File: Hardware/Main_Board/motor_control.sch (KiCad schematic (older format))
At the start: 22 parts

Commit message: [HARDWARE] Complete the SWD design, remove two undrived motor interfaces
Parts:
- removed P? (x2): CONN_4, symbol CONN_4
- removed P? (x2): CONN_6, symbol CONN_6
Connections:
- net labels removed: DIR3, DIR4, MOTOR_EN3, MOTOR_EN4, PWM3, PWM4, enc3_A, enc3_B, enc4_A, enc4_B
- wire segments 120 -> 90
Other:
- moved on the sheet: P?

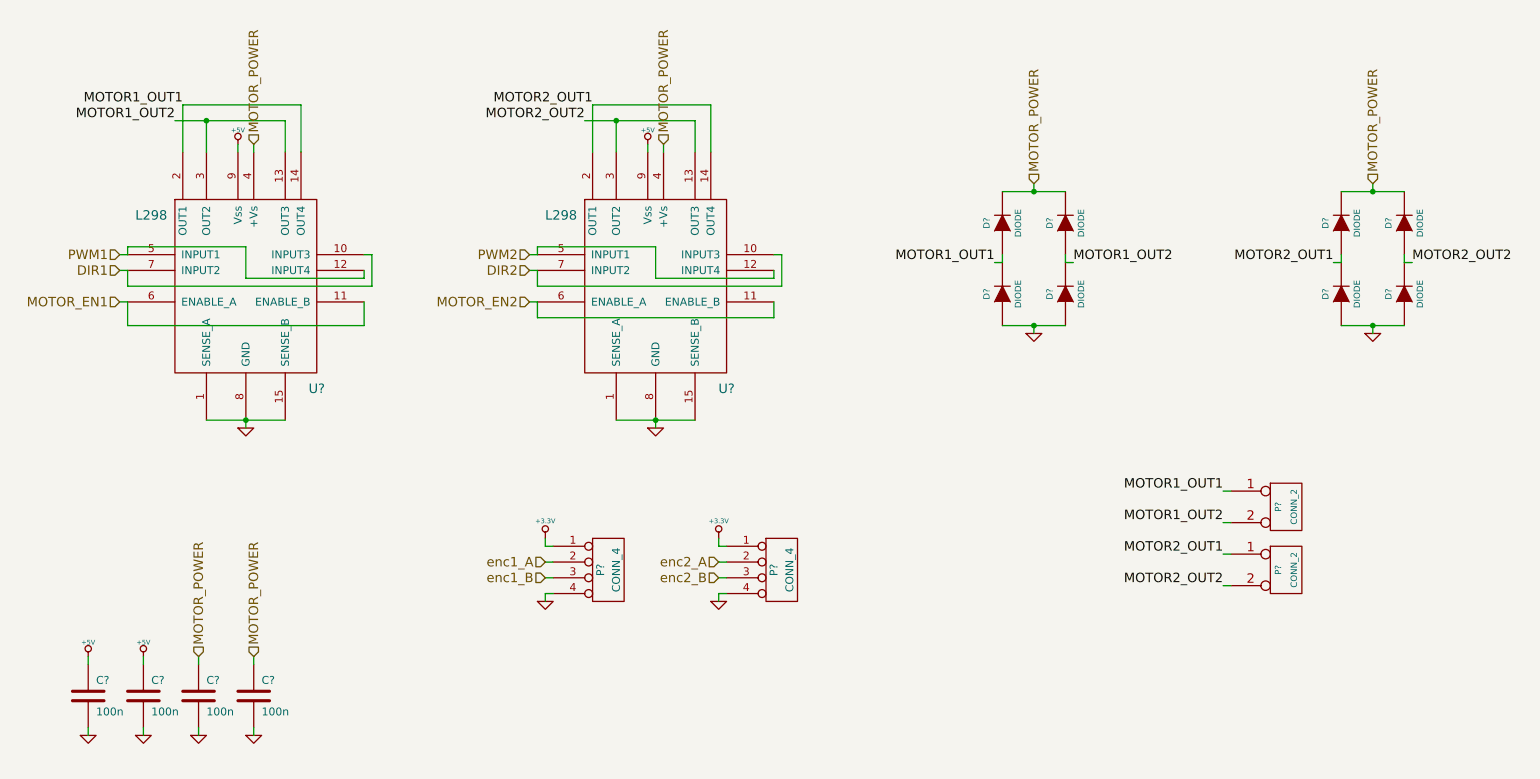
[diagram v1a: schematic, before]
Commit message: [HARDWARE] Component association + schematic modifications
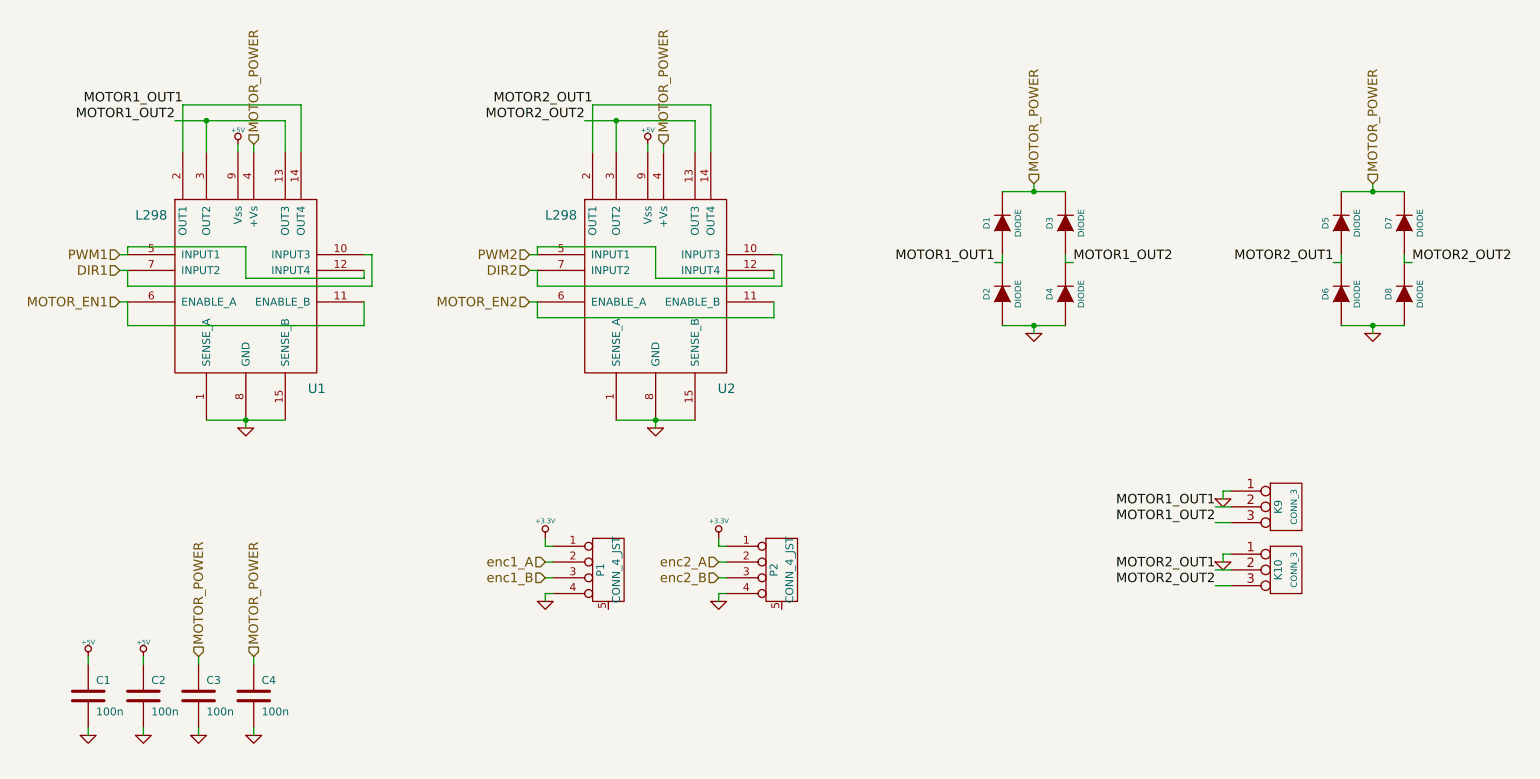
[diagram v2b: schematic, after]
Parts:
- removed P? (x2): CONN_4, symbol CONN_4
- removed P? (x2): CONN_2, symbol CONN_2
- added K10, K9: CONN_3, symbol CONN_3
- added P1, P2: CONN_4_JST, symbol CONN_4_JST
- gave numbers to parts that had none: 14
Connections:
- net +3.3V: now also P1.1 (P1), P2.1 (P1)
- net GND: now also K10.1 (P1), K9.1 (P1), P1.4 (P4), P2.4 (P4)
- net MOTOR1_OUT1: now also K9.2 (PM)
- net MOTOR1_OUT2: now also K9.3 (P3)
- net MOTOR2_OUT1: now also K10.2 (PM)
- net MOTOR2_OUT2: now also K10.3 (P3)
- net enc1_A: now also P1.2 (P2)
- net enc1_B: now also P1.3 (P3)
- net enc2_A: now also P2.2 (P2)
- net enc2_B: now also P2.3 (P3)

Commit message: [HARDWARE] Update schematic and start routing
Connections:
- net GND: now also P1.5 (Shield), P2.5 (Shield)
- net enc1_A: now also P1.3 (P3); no longer P1.2 (P2)
- net enc1_B: now also P1.2 (P2); no longer P1.3 (P3)
- net enc2_A: now also P2.3 (P3); no longer P2.2 (P2)
- net enc2_B: now also P2.2 (P2); no longer P2.3 (P3)

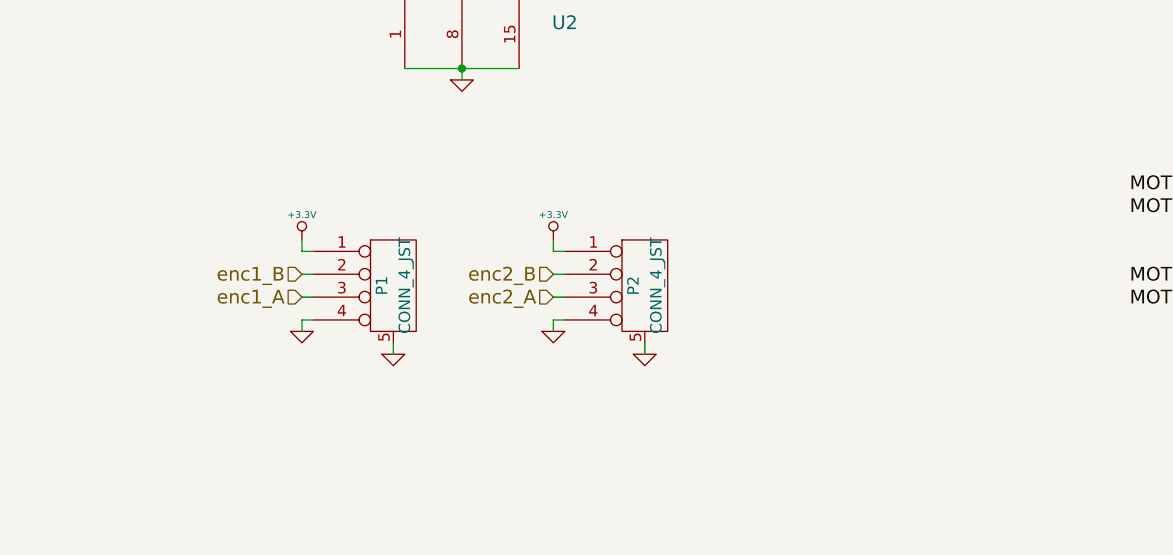
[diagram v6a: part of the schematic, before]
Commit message: [HARDWARE] add pulldown on L298 enable pins, change boot select circuitry, add pullup on USART1, add serigraphy
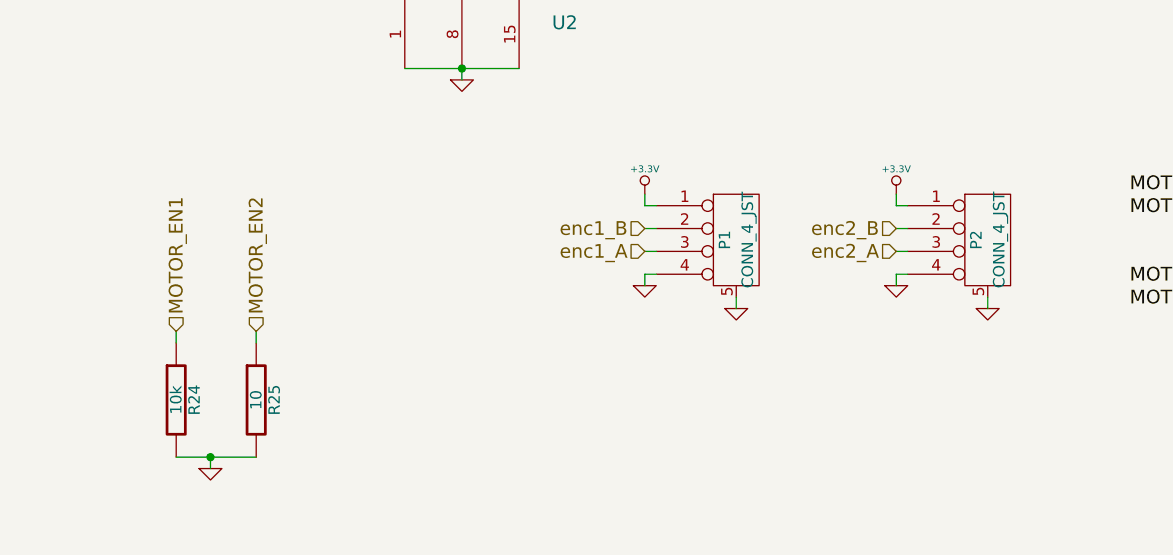
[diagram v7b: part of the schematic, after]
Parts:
- added R24: 10k, symbol R
- added R25: 10, symbol R
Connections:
- net GND: now also R24.2, R25.2
- net MOTOR_EN1: now also R24.1
- net MOTOR_EN2: now also R25.1
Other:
- moved on the sheet: P1, P2
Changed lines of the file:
@@
-EESchema Schematic File Version 2  date dim. 27 oct. 2013 09:44:46 CET
+EESchema Schematic File Version 2  date mar. 17 déc. 2013 16:54:16 CET
 LIBS:power
 LIBS:device
@@
 Sheet 2 6
 Title ""
-Date "27 oct 2013"
+Date "17 dec 2013"
 Rev ""
 Comp ""
@@
 $EndDescr
 Wire Wire Line
-	4650 5100 4650 5050
+	4050 5000 4050 5050
+Connection ~ 3850 5550
+Wire Wire Line
+	3850 5600 3850 5550
+Wire Wire Line
+	6150 4900 6150 4850
 Wire Wire Line
 	8500 4900 8600 4900
@@
 	5000 2150 5000 2100
 Wire Wire Line
-	4300 4750 4250 4750
-Wire Wire Line
-	4300 4950 4250 4950
-Wire Wire Line
-	4250 4950 4250 5000
-Wire Wire Line
-	4250 4600 4250 4650
-Wire Wire Line
-	4250 4650 4300 4650
-Wire Wire Line
-	4250 4850 4300 4850
-Wire Wire Line
-	5350 4850 5400 4850
-Wire Wire Line
-	5400 4650 5350 4650
-Wire Wire Line
-	5350 4650 5350 4600
-Wire Wire Line
-	5350 5000 5350 4950
-Wire Wire Line
-	5350 4950 5400 4950
-Wire Wire Line
-	5400 4750 5350 4750
+	5800 4550 5750 4550
+Wire Wire Line
+	5800 4750 5750 4750
+Wire Wire Line
+	5750 4750 5750 4800
+Wire Wire Line
+	5750 4400 5750 4450
+Wire Wire Line
+	5750 4450 5800 4450
+Wire Wire Line
+	5750 4650 5800 4650
+Wire Wire Line
+	6850 4650 6900 4650
+Wire Wire Line
+	6900 4450 6850 4450
+Wire Wire Line
+	6850 4450 6850 4400
+Wire Wire Line
+	6850 4800 6850 4750
+Wire Wire Line
+	6850 4750 6900 4750
+Wire Wire Line
+	6900 4550 6850 4550
 Wire Wire Line
 	2400 2150 2400 2100
@@
 	8500 4800 8600 4800
 Wire Wire Line
-	5750 5100 5750 5050
+	7250 4900 7250 4850
+Wire Wire Line
+	4050 5550 3700 5550
+Wire Wire Line
+	3700 5000 3700 5050
+Text HLabel 3700 5000 1    60   Input ~ 0
+MOTOR_EN1
+Text HLabel 4050 5000 1    60   Input ~ 0
+MOTOR_EN2
 $Comp
 L GND #PWR01
+U 1 1 52B070BC
+P 3850 5600
+F 0 "#PWR01" H 3850 5600 30  0001 C CNN
+F 1 "GND" H 3850 5530 30  0001 C CNN
+	1    3850 5600
+	1    0    0    -1
+$EndComp
+$Comp
+L R R24
+U 1 1 52B070B1
+P 3700 5300
+F 0 "R24" V 3780 5300 50  0000 C CNN
+F 1 "10k" V 3700 5300 50  0000 C CNN
+	1    3700 5300
+	1    0    0    -1
+$EndComp
+$Comp
+L R R25
+U 1 1 52B070A9
+P 4050 5300
+F 0 "R25" V 4130 5300 50  0000 C CNN
+F 1 "10" V 4050 5300 50  0000 C CNN
+	1    4050 5300
+	1    0    0    -1
+$EndComp
+$Comp
+L GND #PWR02
 U 1 1 526167E5
-P 4650 5100
-F 0 "#PWR01" H 4650 5100 30  0001 C CNN
-F 1 "GND" H 4650 5030 30  0001 C CNN
-	1    4650 5100
-	1    0    0    -1
-$EndComp
-$Comp
-L GND #PWR02
+P 6150 4900
+F 0 "#PWR02" H 6150 4900 30  0001 C CNN
+F 1 "GND" H 6150 4830 30  0001 C CNN
+	1    6150 4900
+	1    0    0    -1
+$EndComp
+$Comp
+L GND #PWR03
 U 1 1 52616798
-P 5750 5100
-F 0 "#PWR02" H 5750 5100 30  0001 C CNN
-F 1 "GND" H 5750 5030 30  0001 C CNN
-	1    5750 5100
+P 7250 4900
+F 0 "#PWR03" H 7250 4900 30  0001 C CNN
+F 1 "GND" H 7250 4830 30  0001 C CNN
+	1    7250 4900
 	1    0    0    -1
 $EndComp
@@
 L CONN_4_JST P2
 U 1 1 525DA05F
-P 5750 4800
-F 0 "P2" V 5700 4800 50  0000 C CNN
-F 1 "CONN_4_JST" V 5800 4800 50  0000 C CNN
-	1    5750 4800
+P 7250 4600
+F 0 "P2" V 7200 4600 50  0000 C CNN
+F 1 "CONN_4_JST" V 7300 4600 50  0000 C CNN
+	1    7250 4600
 	1    0    0    -1
 $EndComp
@@
 L CONN_4_JST P1
 U 1 1 525DA05D
-P 4650 4800
-F 0 "P1" V 4600 4800 50  0000 C CNN
-F 1 "CONN_4_JST" V 4700 4800 50  0000 C CNN
-	1    4650 4800
-	1    0    0    -1
-$EndComp
-$Comp
-L GND #PWR03
+P 6150 4600
+F 0 "P1" V 6100 4600 50  0000 C CNN
+F 1 "CONN_4_JST" V 6200 4600 50  0000 C CNN
+	1    6150 4600
+	1    0    0    -1
+$EndComp
+$Comp
+L GND #PWR04
 U 1 1 525D7EC4
 P 8550 4750
-F 0 "#PWR03" H 8550 4750 30  0001 C CNN
+F 0 "#PWR04" H 8550 4750 30  0001 C CNN
 F 1 "GND" H 8550 4680 30  0001 C CNN
 	1    8550 4750
@@
 $EndComp
 $Comp
-L GND #PWR04
+L GND #PWR05
 U 1 1 525D7EA6
 P 8550 4350
-F 0 "#PWR04" H 8550 4350 30  0001 C CNN
+F 0 "#PWR05" H 8550 4350 30  0001 C CNN
 F 1 "GND" H 8550 4280 30  0001 C CNN
 	1    8550 4350
@@
 MOTOR_POWER
 $Comp
-L GND #PWR05
+L GND #PWR06
 U 1 1 52553CA7
 P 9500 3300
-F 0 "#PWR05" H 9500 3300 30  0001 C CNN
+F 0 "#PWR06" H 9500 3300 30  0001 C CNN
 F 1 "GND" H 9500 3230 30  0001 C CNN
 	1    9500 3300
@@
 MOTOR1_OUT1
 $Comp
-L GND #PWR06
+L GND #PWR07
 U 1 1 52553C7E
 P 7350 3300
-F 0 "#PWR06" H 7350 3300 30  0001 C CNN
+F 0 "#PWR07" H 7350 3300 30  0001 C CNN
 F 1 "GND" H 7350 3230 30  0001 C CNN
 	1    7350 3300
@@
 MOTOR_POWER
 $Comp
-L +5V #PWR07
+L +5V #PWR08
 U 1 1 52553B40
 P 1700 5350
-F 0 "#PWR07" H 1700 5440 20  0001 C CNN
+F 0 "#PWR08" H 1700 5440 20  0001 C CNN
 F 1 "+5V" H 1700 5440 30  0000 C CNN
 	1    1700 5350
@@
 $EndComp
 $Comp
-L +5V #PWR08
+L +5V #PWR09
 U 1 1 52553B3D
 P 1350 5350
-F 0 "#PWR08" H 1350 5440 20  0001 C CNN
+F 0 "#PWR09" H 1350 5440 20  0001 C CNN
 F 1 "+5V" H 1350 5440 30  0000 C CNN
 	1    1350 5350
@@
 $EndComp
 $Comp
-L GND #PWR09
+L GND #PWR010
 U 1 1 52553B3B
 P 2400 5850
-F 0 "#PWR09" H 2400 5850 30  0001 C CNN
+F 0 "#PWR010" H 2400 5850 30  0001 C CNN
 F 1 "GND" H 2400 5780 30  0001 C CNN
 	1    2400 5850
@@
 $EndComp
 $Comp
-L GND #PWR010
+L GND #PWR011
 U 1 1 52553B38
 P 2050 5850
-F 0 "#PWR010" H 2050 5850 30  0001 C CNN
+F 0 "#PWR011" H 2050 5850 30  0001 C CNN
 F 1 "GND" H 2050 5780 30  0001 C CNN
 	1    2050 5850
@@
 $EndComp
 $Comp
-L GND #PWR011
+L GND #PWR012
 U 1 1 52553B36
 P 1700 5850
-F 0 "#PWR011" H 1700 5850 30  0001 C CNN
+F 0 "#PWR012" H 1700 5850 30  0001 C CNN
 F 1 "GND" H 1700 5780 30  0001 C CNN
 	1    1700 5850
@@
 $EndComp
 $Comp
-L GND #PWR012
+L GND #PWR013
 U 1 1 52553B21
 P 1350 5850
-F 0 "#PWR012" H 1350 5850 30  0001 C CNN
+F 0 "#PWR013" H 1350 5850 30  0001 C CNN
 F 1 "GND" H 1350 5780 30  0001 C CNN
 	1    1350 5850
@@
 MOTOR_EN1
 $Comp
-L GND #PWR013
+L GND #PWR014
 U 1 1 52553628
 P 4950 3900
-F 0 "#PWR013" H 4950 3900 30  0001 C CNN
+F 0 "#PWR014" H 4950 3900 30  0001 C CNN
 F 1 "GND" H 4950 3830 30  0001 C CNN
 	1    4950 3900
@@
 $EndComp
 $Comp
-L GND #PWR014
+L GND #PWR015
 U 1 1 52553625
 P 2350 3900
-F 0 "#PWR014" H 2350 3900 30  0001 C CNN
+F 0 "#PWR015" H 2350 3900 30  0001 C CNN
 F 1 "GND" H 2350 3830 30  0001 C CNN
 	1    2350 3900
@@
 $EndComp
 $Comp
-L +5V #PWR015
+L +5V #PWR016
 U 1 1 5255360B
 P 2300 2100
-F 0 "#PWR015" H 2300 2190 20  0001 C CNN
+F 0 "#PWR016" H 2300 2190 20  0001 C CNN
 F 1 "+5V" H 2300 2190 30  0000 C CNN
 	1    2300 2100
@@
 MOTOR_POWER
 $Comp
-L +5V #PWR016
+L +5V #PWR017
 U 1 1 525535E9
 P 4900 2100
-F 0 "#PWR016" H 4900 2190 20  0001 C CNN
+F 0 "#PWR017" H 4900 2190 20  0001 C CNN
 F 1 "+5V" H 4900 2190 30  0000 C CNN
 	1    4900 2100
@@
 $EndComp
 $Comp
-L GND #PWR017
+L GND #PWR018
 U 1 1 52550040
-P 5350 5000
-F 0 "#PWR017" H 5350 5000 30  0001 C CNN
-F 1 "GND" H 5350 4930 30  0001 C CNN
-	1    5350 5000
-	1    0    0    -1
-$EndComp
-$Comp
-L +3.3V #PWR018
+P 6850 4800
+F 0 "#PWR018" H 6850 4800 30  0001 C CNN
+F 1 "GND" H 6850 4730 30  0001 C CNN
+	1    6850 4800
+	1    0    0    -1
+$EndComp
+$Comp
+L +3.3V #PWR019
 U 1 1 5255003F
-P 5350 4600
-F 0 "#PWR018" H 5350 4560 30  0001 C CNN
-F 1 "+3.3V" H 5350 4710 30  0000 C CNN
-	1    5350 4600
-	1    0    0    -1
-$EndComp
-Text HLabel 5350 4850 0    60   Input ~ 0
+P 6850 4400
+F 0 "#PWR019" H 6850 4360 30  0001 C CNN
+F 1 "+3.3V" H 6850 4510 30  0000 C CNN
+	1    6850 4400
+	1    0    0    -1
+$EndComp
+Text HLabel 6850 4650 0    60   Input ~ 0
 enc2_A
-Text HLabel 5350 4750 0    60   Input ~ 0
+Text HLabel 6850 4550 0    60   Input ~ 0
 enc2_B
-Text HLabel 4250 4750 0    60   Input ~ 0
+Text HLabel 5750 4550 0    60   Input ~ 0
 enc1_B
-Text HLabel 4250 4850 0    60   Input ~ 0
+Text HLabel 5750 4650 0    60   Input ~ 0
 enc1_A
 $Comp
-L +3.3V #PWR019
+L +3.3V #PWR020
 U 1 1 5255001D
-P 4250 4600
-F 0 "#PWR019" H 4250 4560 30  0001 C CNN
-F 1 "+3.3V" H 4250 4710 30  0000 C CNN
-	1    4250 4600
-	1    0    0    -1
-$EndComp
-$Comp
-L GND #PWR020
+P 5750 4400
+F 0 "#PWR020" H 5750 4360 30  0001 C CNN
+F 1 "+3.3V" H 5750 4510 30  0000 C CNN
+	1    5750 4400
+	1    0    0    -1
+$EndComp
+$Comp
+L GND #PWR021
 U 1 1 52550018
-P 4250 5000
-F 0 "#PWR020" H 4250 5000 30  0001 C CNN
-F 1 "GND" H 4250 4930 30  0001 C CNN
-	1    4250 5000
-	1    0    0    -1
-$EndComp
+P 5750 4800
+F 0 "#PWR021" H 5750 4800 30  0001 C CNN
+F 1 "GND" H 5750 4730 30  0001 C CNN
+	1    5750 4800
+	1    0    0    -1
+$EndComp
